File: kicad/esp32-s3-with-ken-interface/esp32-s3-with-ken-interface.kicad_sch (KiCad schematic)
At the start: 28 parts, among them J1 TYPE-C-31-M-12, Q1 UMH3N, U1 CH340C, U2 AMS1117-3.3, U3 XDZ254-2-15-W-2.5-G1, U4 ESP32-S3-WROOM-1, U5 PM254-2-15-W-8.5

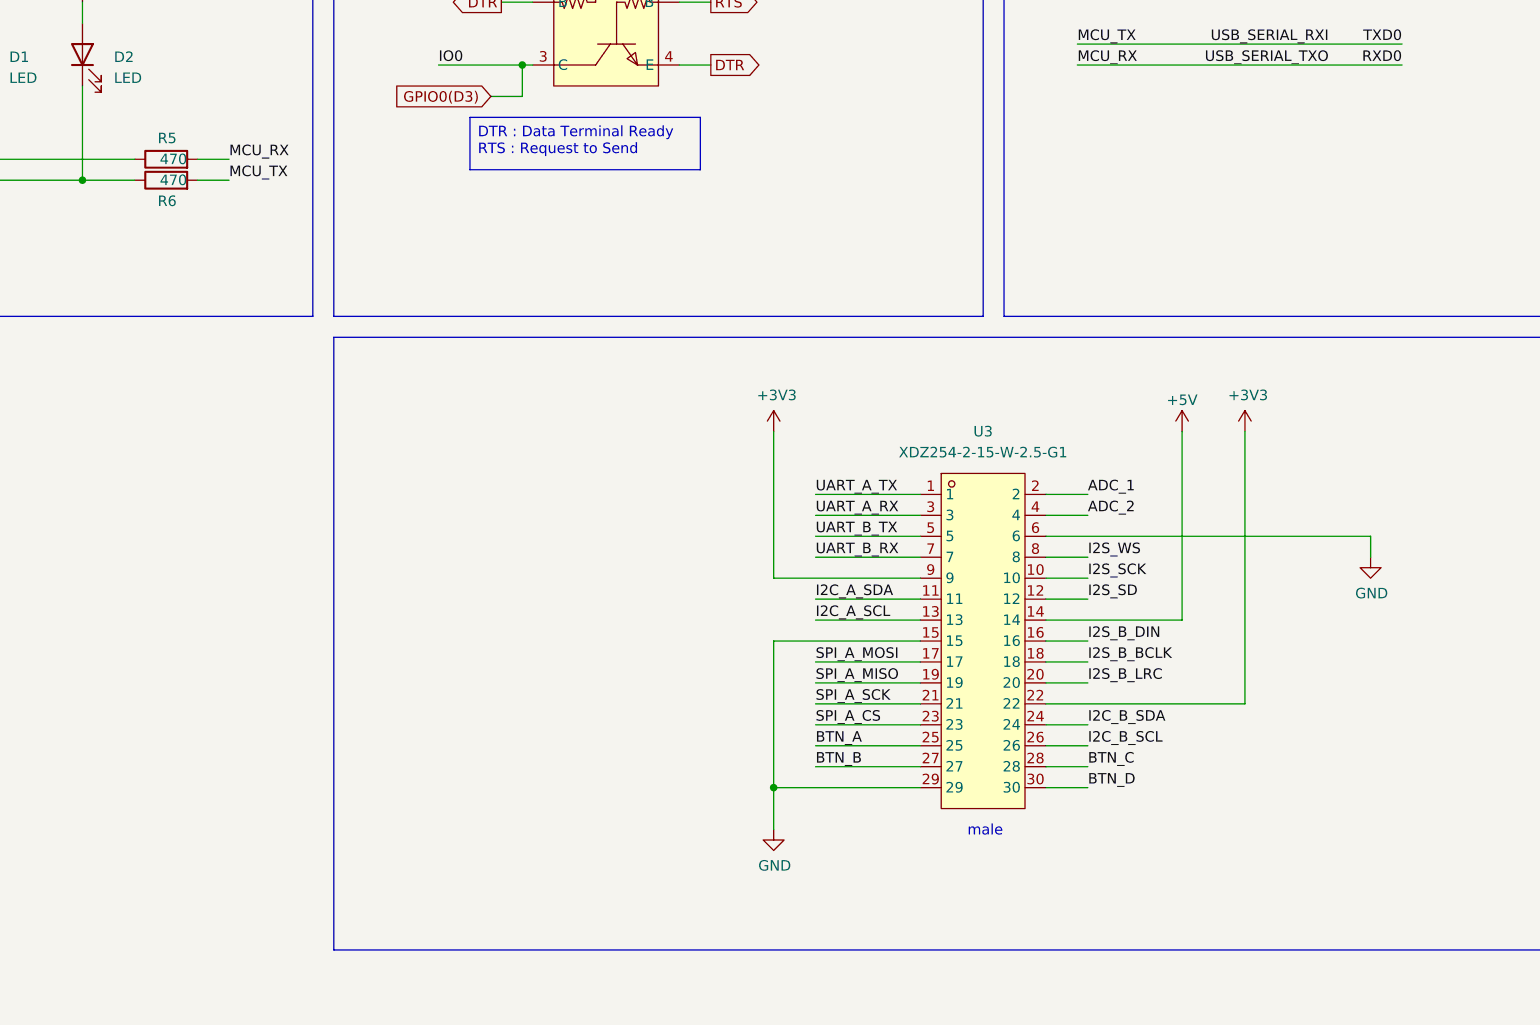
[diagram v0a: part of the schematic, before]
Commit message: fix left pin header pin assignment
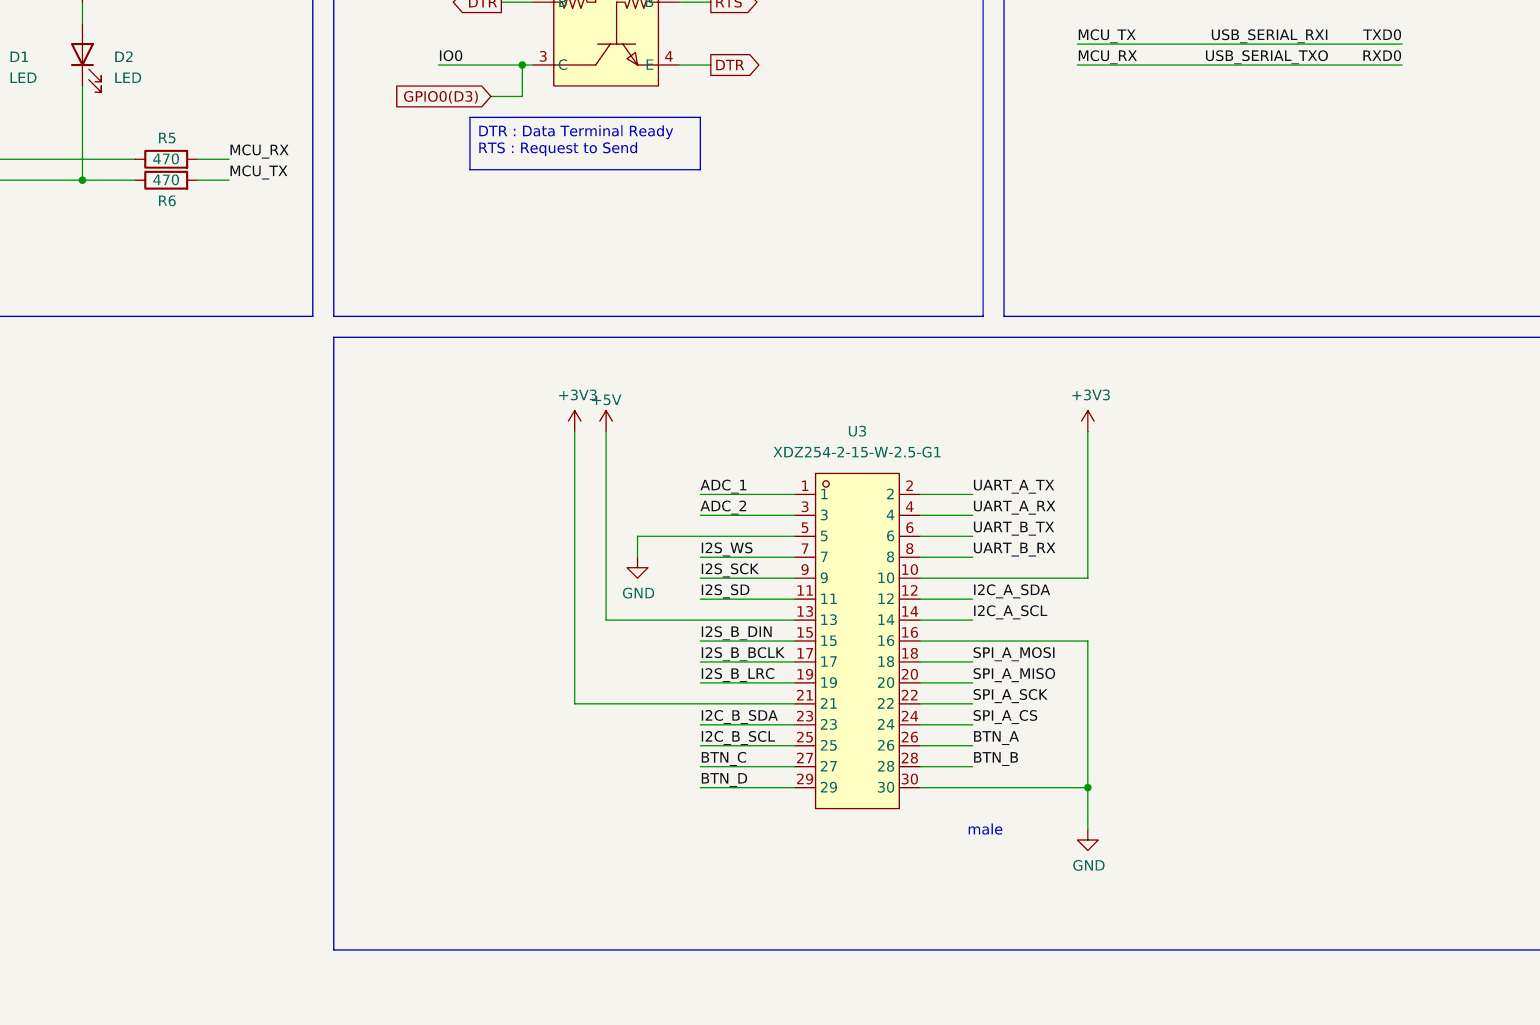
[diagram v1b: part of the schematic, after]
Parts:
- D1, D2: footprint LED_SMD:LED_1206_3216Metric -> LED_SMD:LED_1206_3216Metric_Pad1.42x1.75mm_HandSolder
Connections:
- net +3V3: now also U3.10, U3.21; no longer U3.22, U3.9
- net +5V: now also U3.13; no longer U3.14
- net ADC_1: now also U3.1; no longer U3.2
- net ADC_2: now also U3.3; no longer U3.4
- net BTN_A: now also U3.26; no longer U3.25
- net BTN_B: now also U3.28; no longer U3.27
- net BTN_C: now also U3.27; no longer U3.28
- net BTN_D: now also U3.29; no longer U3.30
- net GND: now also U3.16, U3.30, U3.5; no longer U3.15, U3.29, U3.6
- net I2C_A_SCL: now also U3.14; no longer U3.13
- net I2C_A_SDA: now also U3.12; no longer U3.11
- net I2C_B_SCL: now also U3.25; no longer U3.26
- net I2C_B_SDA: now also U3.23; no longer U3.24
- net I2S_B_BCLK: now also U3.17; no longer U3.18
- net I2S_B_DIN: now also U3.15; no longer U3.16
- net I2S_B_LRC: now also U3.19; no longer U3.20
- net I2S_SCK: now also U3.9; no longer U3.10
- net I2S_SD: now also U3.11; no longer U3.12
- net I2S_WS: now also U3.7; no longer U3.8
- net IO10: now also U3.24; no longer U3.23
- net IO11: now also U3.18; no longer U3.17
- net IO12: now also U3.22; no longer U3.21
- net IO13: now also U3.20; no longer U3.19
- net IO17: now also U3.2; no longer U3.1
- net IO18: now also U3.4; no longer U3.3
- net IO19: now also U3.6; no longer U3.5
- net IO20: now also U3.8; no longer U3.7

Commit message: add pin label, adjust routing, add PWM pins
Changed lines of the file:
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@@
 		)
 	)
-	(label "IO7"
+	(label "IO40"
 		(at 44.45 205.74 0)
 		(effects
@@
 		)
 	)
-	(label "IO17"
+	(label "IO41"
 		(at 44.45 209.55 0)
 		(effects
@@
 		)
 	)
-	(label "IO18"
+	(label "IO39"
 		(at 44.45 201.93 0)
 		(effects
@@
 		)
 	)
-	(label "IO15"
+	(label "IO42"
 		(at 44.45 213.36 0)
 		(effects
@@
 		)
 	)
-	(label "IO8"
+	(label "IO14"
 		(at 44.45 194.31 0)
 		(effects
@@
 		)
 	)
-	(label "IO16"
+	(label "IO21"
 		(at 44.45 198.12 0)
 		(effects

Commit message: add protect diode, improve trace routing, add vias, add user button and user led, improve schematic, add texts
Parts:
- added D3: LED, LED_SMD:LED_1206_3216Metric_Pad1.42x1.75mm_HandSolder, symbol Device:LED
- added D4: B5819W_C109213, B5819W:SOD-123_L2.8-W1.8-LS3.7-RD, symbol B5819W:B5819W_C109213
- added R8: 1k, Resistor_SMD:R_0603_1608Metric_Pad0.98x0.95mm_HandSolder, symbol Device:R
- added SW1: TSC015A03526A, TSC015A03526A:SW-SMD_4P-L4.5-W4.5-P3.00-LS6.8, symbol TSC015A03526A:TSC015A03526A
- C2, C5: footprint Capacitor_SMD:C_0805_2012Metric_Pad1.18x1.45mm_HandSolder -> Capacitor_SMD:C_1206_3216Metric_Pad1.33x1.80mm_HandSolder
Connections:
- net +5V: now also D4.1 (K); no longer J1.A4B9 (VBUS), J1.B4A9 (VBUS)
- net GND: now also D3.1 (K), SW1.3, SW1.4
- net IO47: now also R8.1
- net IO48: now also SW1.2
- net GPIO0(D3) renamed ESP32_BOOT
- net RESET renamed EN
- new net: D3.2 (A), R8.2
- new net VBUS: D4.2 (A), J1.A4B9 (VBUS), J1.B4A9 (VBUS)
- no-connect marks 11 -> 12
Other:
- note added: "BASIC PIN ASSIGNMENT"
- note added: "ESP32-S3-WROOM-1"
- note added: "KEN INTERFACE"
- note added: "OPTIONS"
- note added: "bit clock"
- note added: "clock"
- note added: "digital input"
- note added: "for MAX98357A, etc."
- note added: "for oled, etc. option"
- note added: "left male"
- note added: "left right clock"
- note added: "options (or just use pwm pins)"
- note added: "right female"
- note added: "serial data"
- note added: "word select"
- note removed: "for oled, etc."
- moved on the sheet: C6, D1, D2, R3, R4, R5, R7, U3, U5

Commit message: improve schematic and trace routing, improve silk text, etc
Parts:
- removed C2, C5: 10uF, Capacitor_SMD:C_1206_3216Metric_Pad1.33x1.80mm_HandSolder, symbol Device:C_Small
- removed C6: 1uF, Capacitor_SMD:C_0603_1608Metric_Pad1.08x0.95mm_HandSolder, symbol Device:C_Small
- added C2, C5: 10uF, Capacitor_SMD:C_1206_3216Metric_Pad1.33x1.80mm_HandSolder, symbol Device:C
- added C6: 1uF, Capacitor_SMD:C_0603_1608Metric_Pad1.08x0.95mm_HandSolder, symbol Device:C
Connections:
- net +3V3: now also C5.1
- net +5V: now also C2.1
- net EN: now also C6.1
- net GND: now also C2.2, C5.2, C6.2
- net ESP32_BOOT renamed IO0
- net I2S_SCK renamed I2S_A_SCK
- net I2S_SD renamed I2S_A_SD
- net I2S_WS renamed I2S_A_WS
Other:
- note added: "MOUNT HOLES"
- note added: "RTS( from CH340C)! NOT RST from MCU pay attention!"
- note added: "serial clock"
- note removed: "MECHANICAL/BOM-ONLY"
- note removed: "clock"
- note removed: "mcu RST! not RTS( from CH340C)! pay attention!"
- moved on the sheet: C1, C3, C4, D4, H1, H2, H3, H4, J1, Q1, R1, R2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

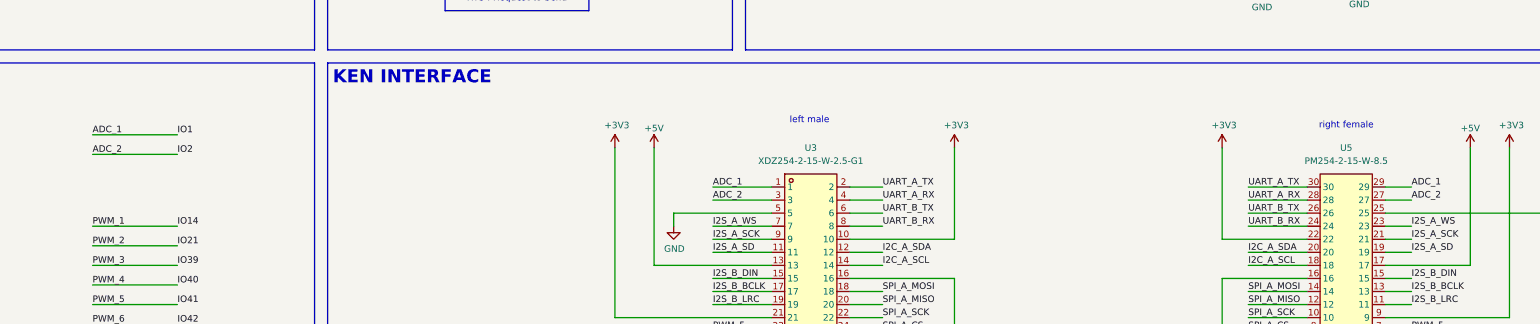
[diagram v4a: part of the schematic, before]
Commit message: rename ADC_1 to ADC_A, ADC_2 to ADC_B,also update the silk text
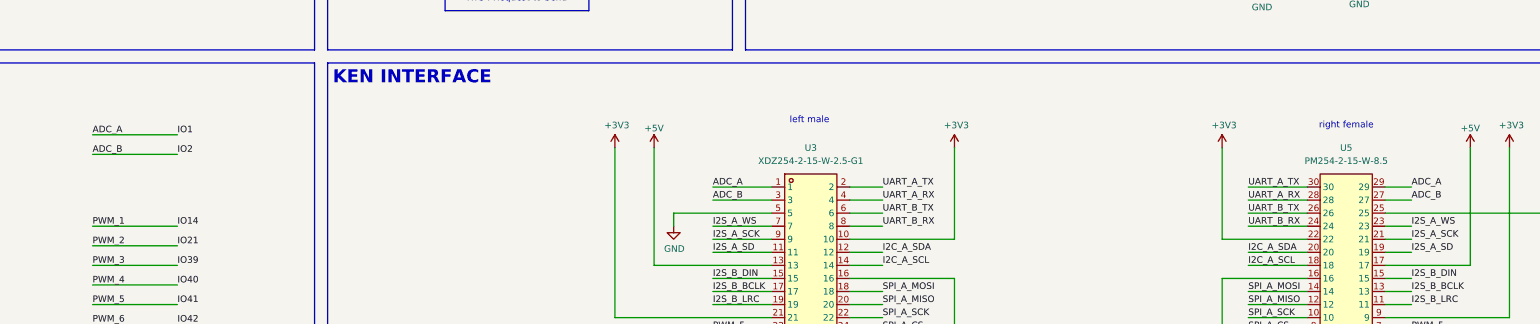
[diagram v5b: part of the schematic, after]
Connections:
- net ADC_1 renamed ADC_A
- net ADC_2 renamed ADC_B
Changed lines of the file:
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@@
 		)
 	)
-	(label "ADC_2"
+	(label "ADC_B"
 		(at 85.09 146.05 0)
 		(effects
@@
 		)
 	)
-	(label "ADC_1"
+	(label "ADC_A"
 		(at 205.74 152.4 0)
 		(effects
@@
 		)
 	)
-	(label "ADC_2"
+	(label "ADC_B"
 		(at 341.63 154.94 0)
 		(effects
@@
 		)
 	)
-	(label "ADC_2"
+	(label "ADC_B"
 		(at 205.74 154.94 0)
 		(effects
@@
 		)
 	)
-	(label "ADC_1"
+	(label "ADC_A"
 		(at 341.63 152.4 0)
 		(effects
@@
 		)
 	)
-	(label "ADC_1"
+	(label "ADC_A"
 		(at 85.09 142.24 0)
 		(effects
